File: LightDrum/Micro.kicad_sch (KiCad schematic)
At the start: 22 parts, among them J1 SWD CONN, SW1 BOOT0, Y1 16MHz, Y2 32.768KHz

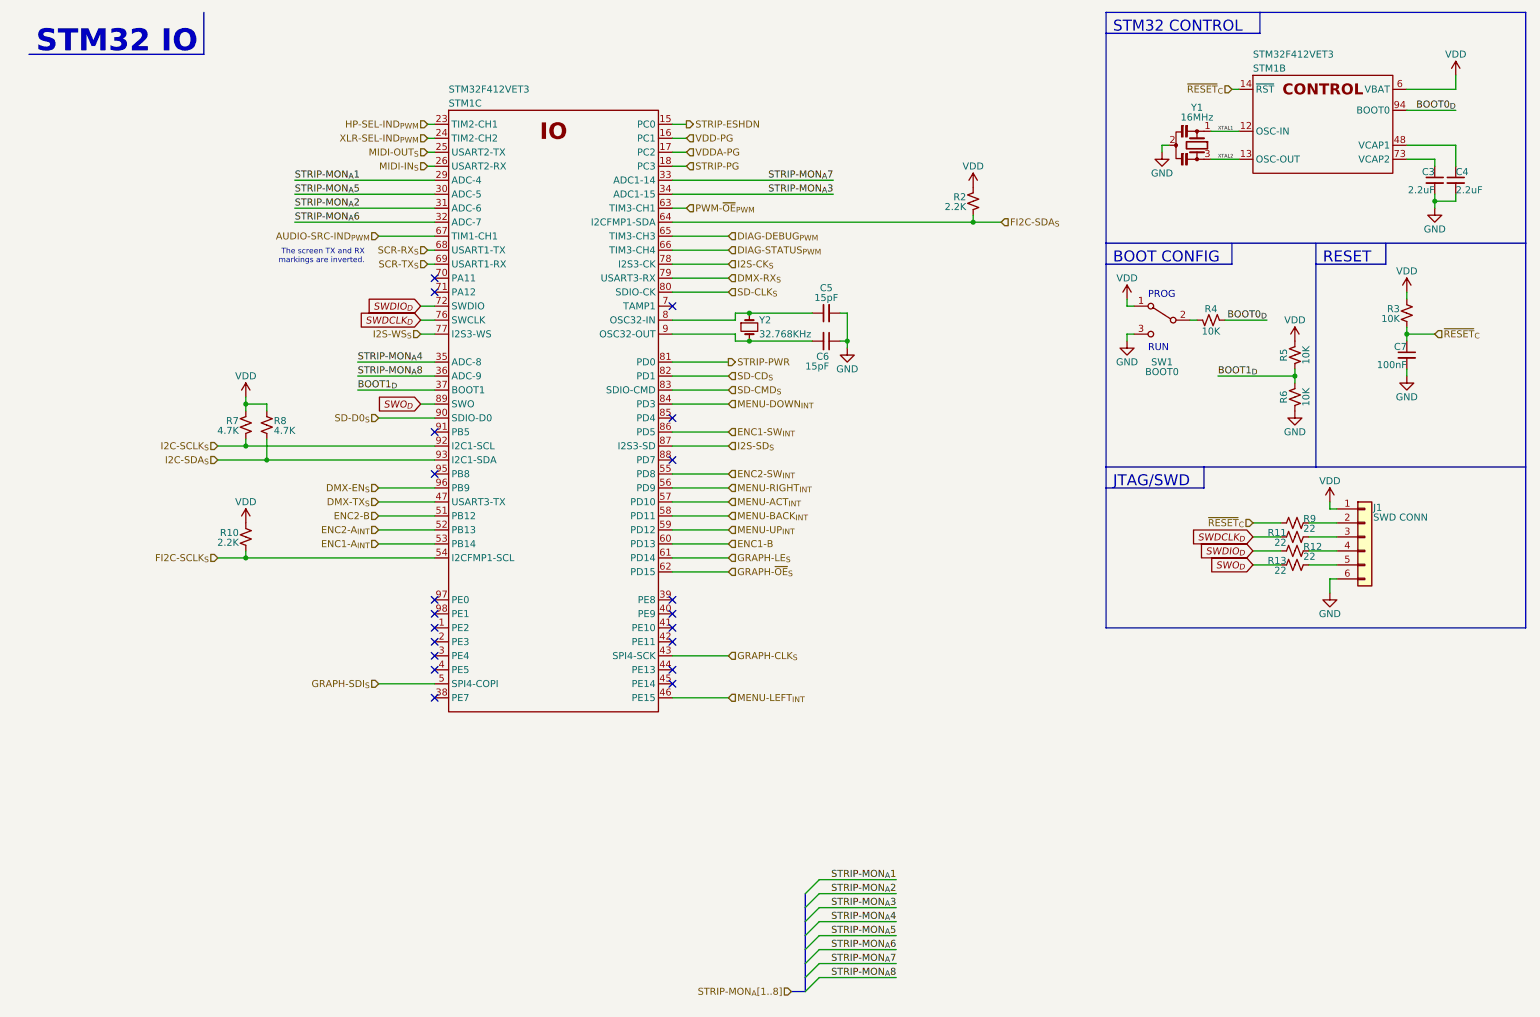
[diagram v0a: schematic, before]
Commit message: Replace DSub with much better ECU conn
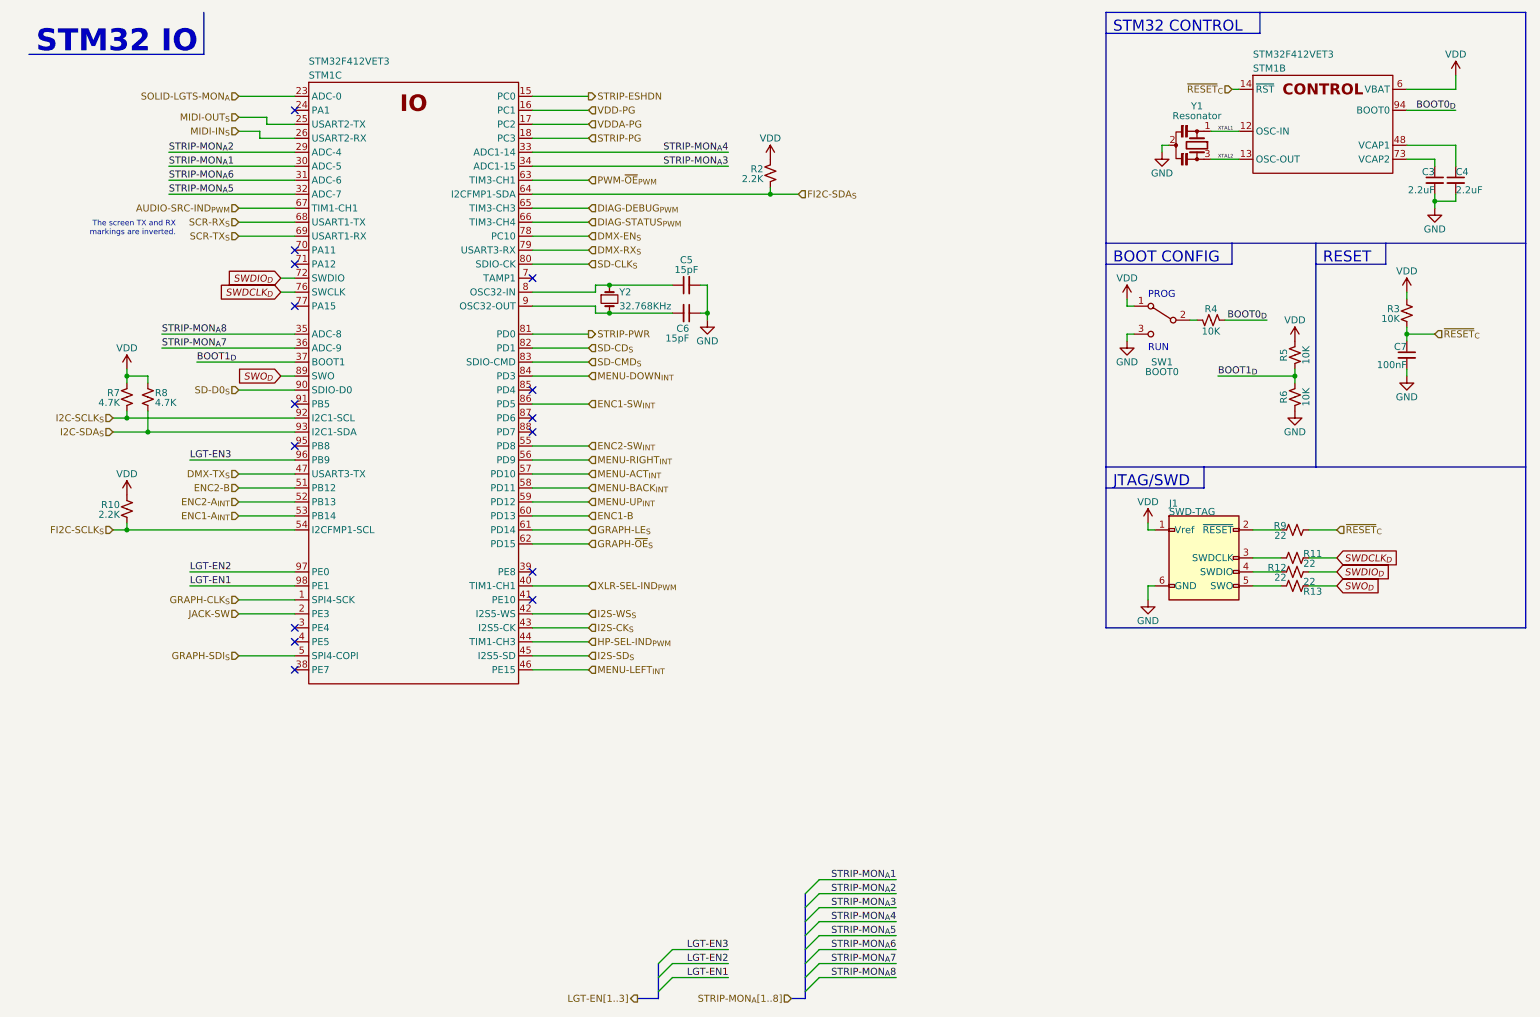
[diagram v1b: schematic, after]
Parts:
- removed J1: SWD CONN, Connector_PinHeader_1.27mm:PinHeader_1x06_P1.27mm_Vertical, symbol Connector_Generic:Conn_01x06
- removed Y1: 16MHz, Crystal:Resonator_SMD_Murata_CSTxExxV-3Pin_3.0x1.1mm, symbol Device:Resonator_Small
- added J1: SWD-TAG, Daxxn_Connectors:903250006, symbol Daxxn_Connectors:SWD-TAG-2
- added Y1: Resonator, Daxxn_Passives:Resonator_SMD_3Pin_3.0x1.1mm, symbol Daxxn_Device:Resonator
- STM1: footprint Package_QFP:LQFP-100_14x14mm_P0.5mm -> Daxxn_Packages:LQFP-100_14x14mm_P0.5mm
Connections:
- net DMX-EN_{S}: now also STM1.78 (PC10); no longer STM1.96 (PB9)
- net GND: now also J1.6 (GND), Y1.2
- net GRAPH-CLK_{S}: now also STM1.1 (PE2); no longer STM1.43 (PE12)
- net HP-SEL-IND_{PWM}: now also STM1.44 (PE13); no longer STM1.23 (PA0)
- net I2S-CK_{S}: now also STM1.43 (PE12); no longer STM1.78 (PC10)
- net I2S-SD_{S}: now also STM1.45 (PE14); no longer STM1.87 (PD6)
- net I2S-WS_{S}: now also STM1.42 (PE11); no longer STM1.77 (PA15)
- net STRIP-MON_{A}1: now also STM1.30 (PA5); no longer STM1.29 (PA4)
- net STRIP-MON_{A}2: now also STM1.29 (PA4); no longer STM1.31 (PA6)
- net STRIP-MON_{A}4: now also STM1.33 (PC4); no longer STM1.35 (PB0)
- net STRIP-MON_{A}5: now also STM1.32 (PA7); no longer STM1.30 (PA5)
- net STRIP-MON_{A}6: now also STM1.31 (PA6); no longer STM1.32 (PA7)
- net STRIP-MON_{A}7: now also STM1.36 (PB1); no longer STM1.33 (PC4)
- net STRIP-MON_{A}8: now also STM1.35 (PB0); no longer STM1.36 (PB1)
- net SWDCLK_{D}: now also R11.2; no longer R11.1
- net VDD: now also J1.1 (Vref)
- net XLR-SEL-IND_{PWM}: now also STM1.40 (PE9); no longer STM1.24 (PA1)
- net XTAL1: now also Y1.1
- net XTAL2: now also Y1.3
- net JACK-SW: now reaches STM1.2 (PE3)
- net LGT-EN2: now reaches STM1.97 (PE0)
- net LGT-EN1: now reaches STM1.98 (PE1)
- net at R9.2: now also J1.2 (~{RESET})
- net at R12.2: now also J1.4 (SWDIO)
- net at R13.2: now also J1.5 (SWO)
- new net: J1.3 (SWDCLK), R11.1
- new net LGT-EN3: STM1.96 (PB9)
- new net SOLID-LGTS-MON_{A}: STM1.23 (PA0)
- no-connect marks 20 -> 15
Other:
- moved on the sheet: C5, C6, R10, R11, R12, R13, R2, R7, R8, R9, STM1C, Y2

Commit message: Organize old files and generate interface gerbers
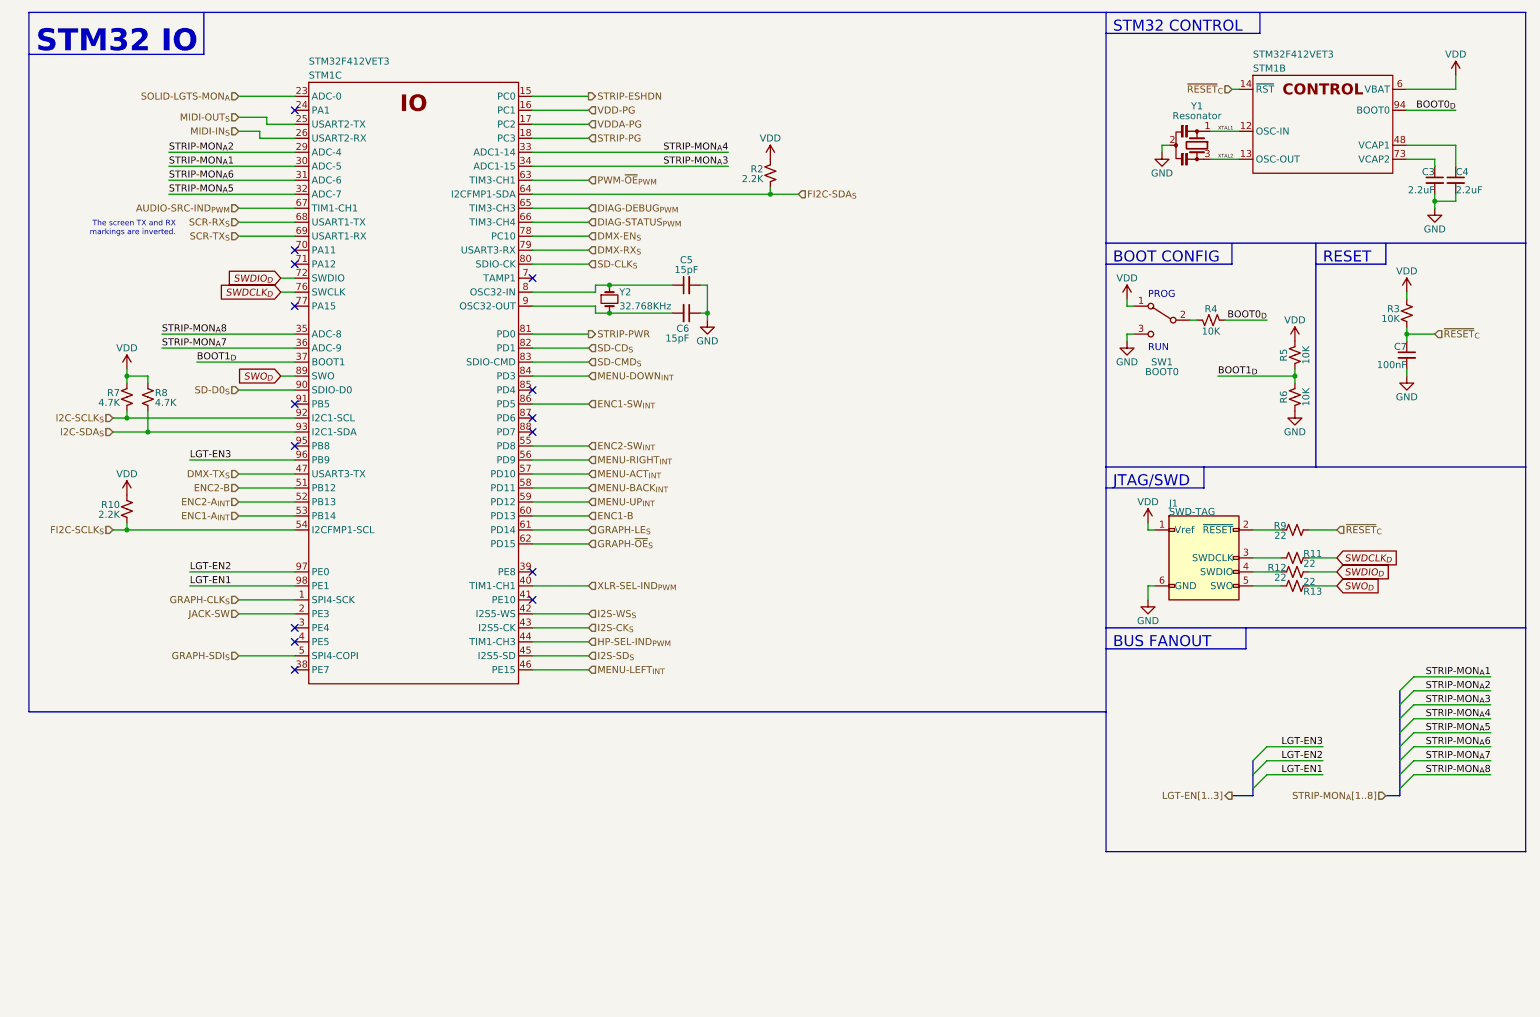
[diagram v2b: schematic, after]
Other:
- note added: "BUS FANOUT"

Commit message: Fix schematic layout
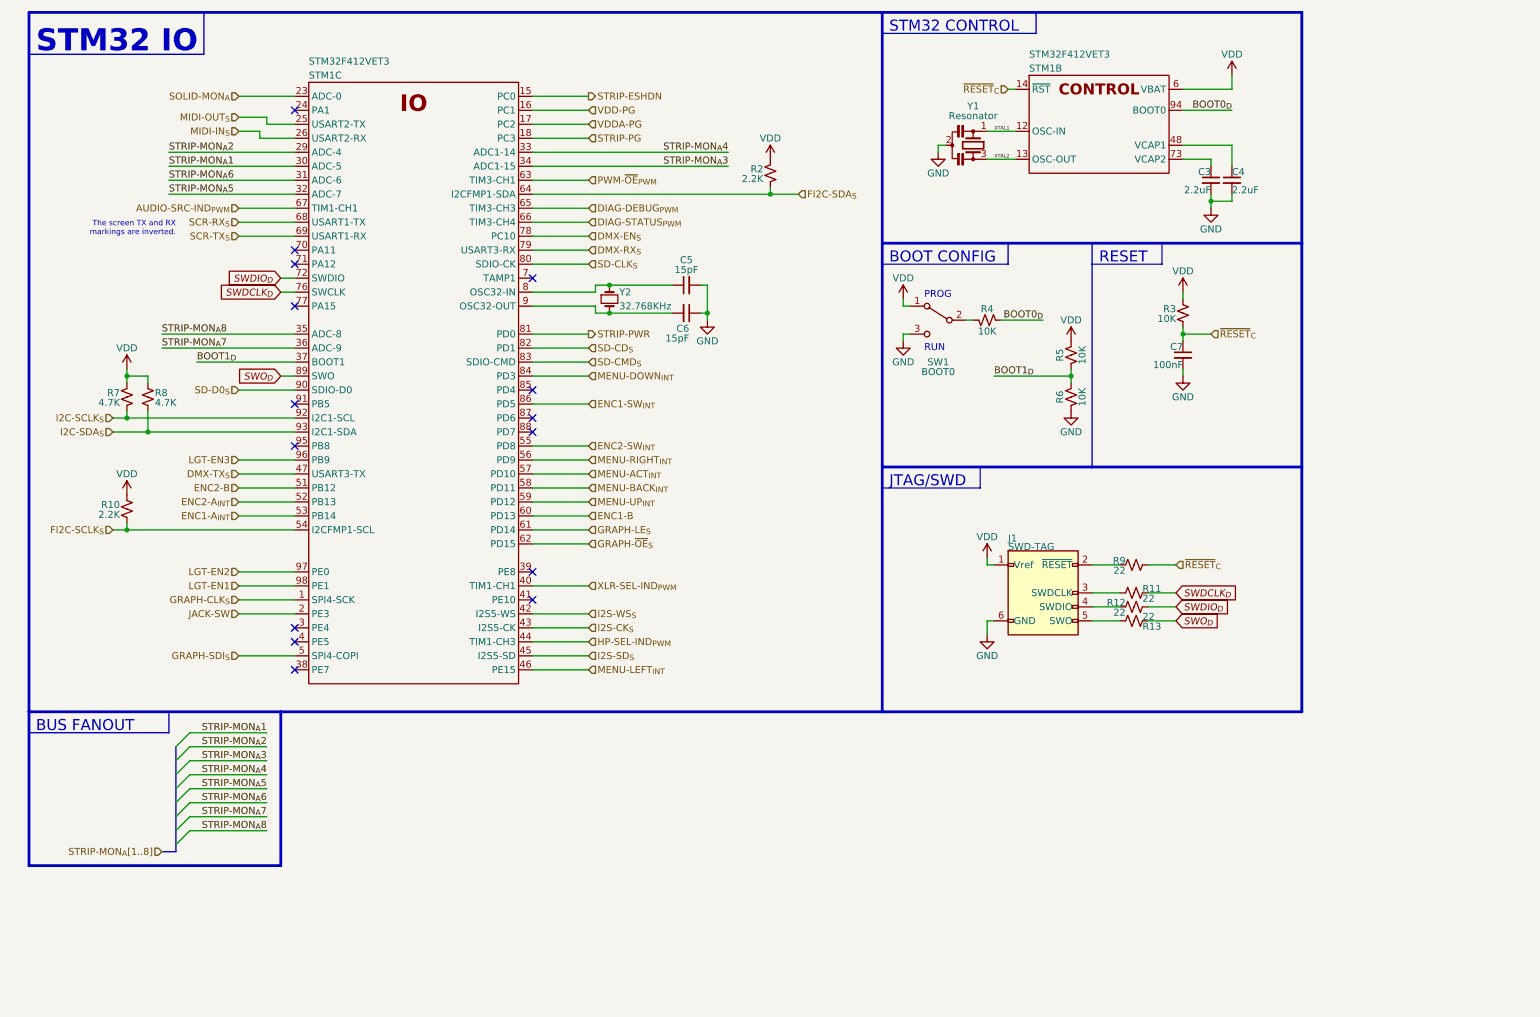
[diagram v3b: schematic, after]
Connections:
- net SOLID-LGTS-MON_{A} renamed SOLID-MON_{A}
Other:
- moved on the sheet: C3, C4, C7, J1, R11, R12, R13, R3, R4, R5, R6, R9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
